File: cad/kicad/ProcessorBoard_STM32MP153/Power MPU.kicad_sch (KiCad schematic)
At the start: 1 part, among them IC301 STPMIC1BPQR

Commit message: some more caps and power specs
maybe puppy and rainbows if dont use the sw controlled PMIC. ddr dosent seem to care too much about sequencing, and the mpu sequence is 2 steps... but size :( :( :( . wheres muh leaded puckagies :(
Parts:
- added C301, C303, C305, C307: 10u, Capacitor_SMD:C_0603_1608Metric_Pad1.08x0.95mm_HandSolder, symbol Device:C_Small
- added C302, C304, C306, C308: 22u, Capacitor_SMD:C_0603_1608Metric_Pad1.08x0.95mm_HandSolder, symbol Device:C_Small
- added C309, C310, C311, C312, C313, C314: 1u, Capacitor_SMD:C_0603_1608Metric_Pad1.08x0.95mm_HandSolder, symbol Device:C_Small
- added L301, L302, L303, L304: 1u, Inductor_SMD:L_1008_2520Metric_Pad1.43x2.20mm_HandSolder, symbol Device:L_Small
- added NT301, NT302, NT303, NT304: NetTie_2, NetTie:NetTie-2_SMD_Pad0.5mm, symbol Device:NetTie_2
- added R301, R302: 3090, Resistor_SMD:R_0603_1608Metric_Pad0.98x0.95mm_HandSolder, symbol Device:R_Small_US
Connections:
- net LDO2in is gone; now on net 3v3: IC301.19 (LDO25IN)
- net SWin is gone; now on net BoostOut: IC301.37 (SWIN)
- net GND: now also C301.2, C302.2, C303.2, C304.2, C305.2, C306.2, C307.2, C308.2, C309.2, C310.2, C311.1, C312.2, C313.2, C314.1
- net LDO2out: now also C314.2
- net LDO5out: now also C313.1
- net LDO6out: now also C311.2
- net SCL: now also R301.2
- net SDA: now also R302.1
- net VLX1: now also L301.2
- net VLX2: now also L302.2
- net Vin_prim: now also C301.1, C303.1, C305.1, C307.1
- net Vout3FB: now also NT303.1
- net Vout4FB: now also NT304.1
- net LDO1and6in renamed 3v3
- net 3v3: now also C302.1, C309.1, C312.1, L304.1, NT304.2
- net LSO1out renamed LDO1out
- net LDO1out: now also C310.1
- net VLXBuck3 renamed VLX3
- net VLX3: now also L303.2
- net VLXBuck4 renamed VLX4
- net VLX4: now also L304.2
- net Vio renamed VddIO
- net VddIO: now also R301.1, R302.2
- net Vout1 renamed Vout1FB
- net Vout1FB: now also NT301.1
- net Vout2 renamed Vout2FB
- net Vout2FB: now also NT302.1
- new net V_{dd_DDR}: C306.1, L302.1, NT302.2
- new net V_{dd_IO}: C304.1, L303.1, NT303.2
- new net V_{dd_core}: C308.1, L301.1, NT301.2
- no-connect marks 0 -> 2
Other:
- note added: "unused. programmable out: [0v9,3v3], %2, 100mV steps"
- note added: "unused. programmable out: [1v8,3v3], %2, 100mV steps"

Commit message: pmic maybe
caybe bees in the halls of 3d objects. post gimp utility. hp bug kit
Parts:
- added C315, C319, C320: 10u, Capacitor_SMD:C_0603_1608Metric_Pad1.08x0.95mm_HandSolder, symbol Device:C_Small
- added C316, C317, C318, C321: 1u, Capacitor_SMD:C_0603_1608Metric_Pad1.08x0.95mm_HandSolder, symbol Device:C_Small
- added J301: Conn_01x01_Pin, Connector_PinHeader_2.54mm:PinHeader_1x01_P2.54mm_Vertical, symbol Connector:Conn_01x01_Pin
- added L305: 1u, Inductor_SMD:L_1008_2520Metric_Pad1.43x2.20mm_HandSolder, symbol Device:L_Small
- C311, C314: now not fitted; now left out of the parts list
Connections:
- net VddIO is gone; now on net V_{dd_IO}: IC301.42 (VIO), R301.1, R302.2
- net GND: now also C315.2, C316.2, C317.2, C318.2, C319.2, C320.2, C321.2
- net LDO3in: now also C308.1, L301.1, NT303.2, C319.1
- net LDO3out: now also C320.1
- net LDO4out: now also C318.1
- net PonkeyN: now also J301.1 (Pin_1)
- net VBusOTG: now also C316.1
- net VLXBoost: now also L305.1
- net V_{dd_IO}: now also NT301.2; no longer NT303.2
- net Vin_prim: now also C315.1, C317.1, L305.2
- net Vout1FB: now also NT303.1; no longer NT301.1
- net Vout3FB: now also NT301.1; no longer NT303.1
- net BoostOut: no longer names the net of IC301.34 (BOUT)
- net BoostOut: no longer IC301.37 (SWIN)
- net SWout: no longer names the net of IC301.38 (SWOUT)
- net V_{dd_DDR} renamed V_{dd_DDRQ}
- removed net V_{dd_core}: C308.1, L301.1, NT301.2
- net VrefDDR renamed V_{DDR_ref}
- net V_{DDR_ref}: now also C321.1
- no-connect marks 2 -> 5
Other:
- note added: "what to do with unused pins"
- moved on the sheet: C301, C302, C303, C304, C305, C306, C307, C308, C309, C310, C312, C313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

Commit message: respeced caps
everything out of stok :(
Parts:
- added C322, C323: 4.7u, Capacitor_SMD:C_01005_0402Metric_Pad0.57x0.30mm_HandSolder, symbol Device:C_Small
- added C324: 1u, Capacitor_SMD:C_01005_0402Metric_Pad0.57x0.30mm_HandSolder, symbol Device:C_Small
- C309, C312, C316, C317, C321: footprint Capacitor_SMD:C_0603_1608Metric_Pad1.08x0.95mm_HandSolder -> Capacitor_SMD:C_01005_0402Metric_Pad0.57x0.30mm_HandSolder; character https://ds.yuden.co.jp/TYCOMPAS/ap/detail?pn=MSASE168SB7105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 -> https://ds.murata.com/simsurfing/mlcc.html?partnumbers=%5B%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; mouser https://www.mouser.com/en/ProductDetail/Samsung-Electro-Mec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 -> https://www.mouser.com/en/ProductDetail/Murata-Electronics/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; unit x1 0.29 -> 0.11; unit x10 0.168 -> 0.04
- C310, C311, C313, C314, C318: value 1u -> 4.7u; footprint Capacitor_SMD:C_0603_1608Metric_Pad1.08x0.95mm_HandSolder -> Capacitor_SMD:C_01005_0402Metric_Pad0.57x0.30mm_HandSolder; character https://ds.yuden.co.jp/TYCOMPAS/ap/detail?pn=MSASE168SB7105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 -> https://ds.murata.com/simsurfing/mlcc.html?partnumbers=%5B%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; mouser https://www.mouser.com/en/ProductDetail/Samsung-Electro-Mec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 -> https://www.mouser.com/en/ProductDetail/Murata-Electronics/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; unit x1 0.29 -> 0.047; unit x10 0.168 -> 0.11
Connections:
- net AGnd is gone; now on net GND: IC301.41 (AGND)
- net GND: now also C311.2, C314.2, C322.2, C323.2, C324.2; no longer C311.1, C314.1
- net InternalLDO: now also C323.1
- net LDO2out: now also C314.1; no longer C314.2
- net LDO6out: now also C311.1; no longer C311.2
- net VBusOTG: now also C324.1
- net Vin_prim: now also C322.1
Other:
- moved on the sheet: IC301, J301, R301, R302

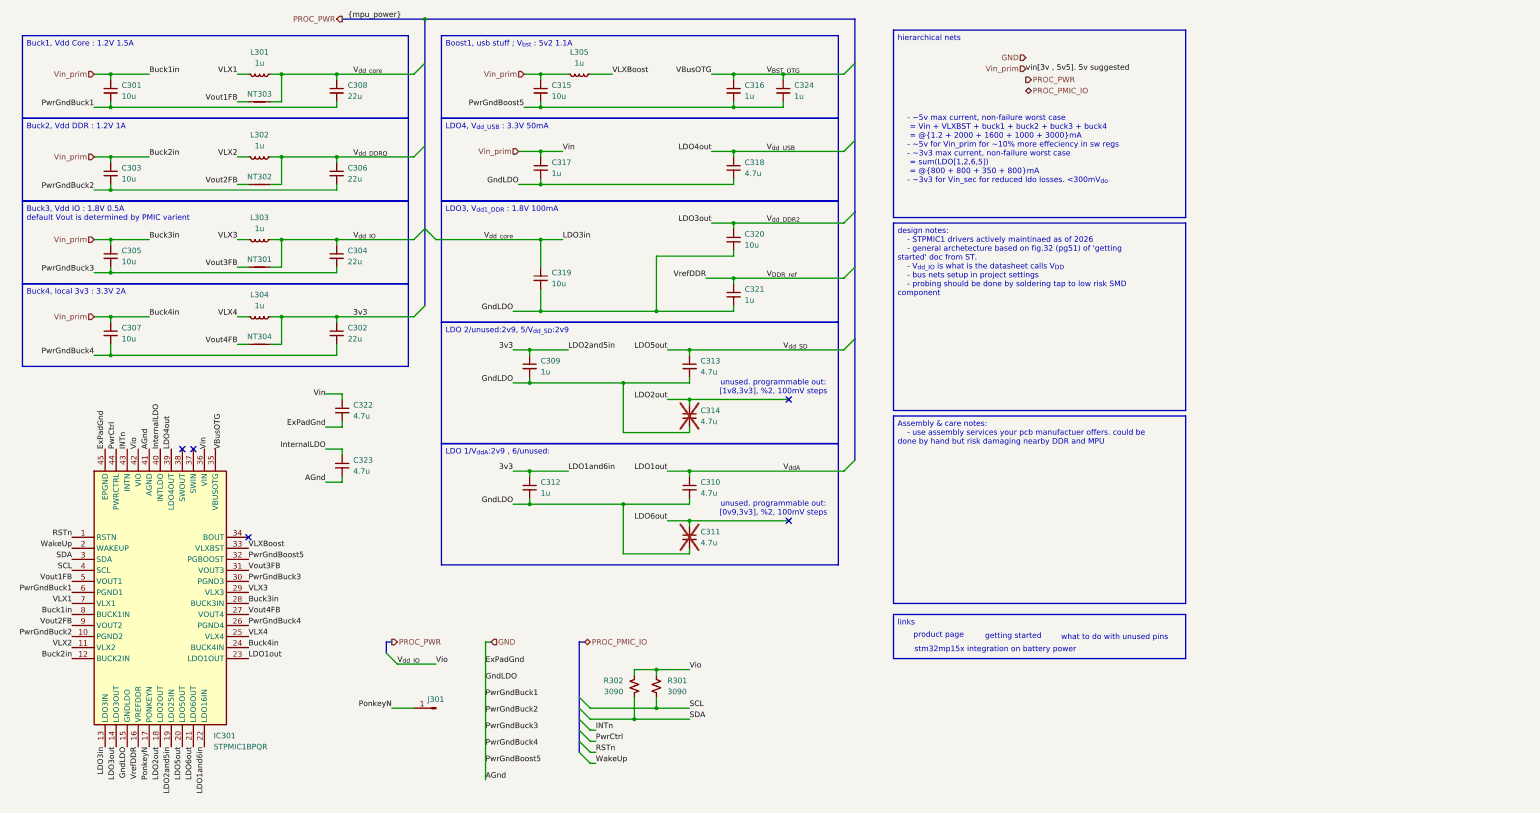
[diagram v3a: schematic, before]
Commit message: verified jlc price category
~[32, 50]usd for 5 boards. includes impedence control. though must be 1oz top & bottom layers, 0.5oz inner layers . goes up at least $10usd for different pours
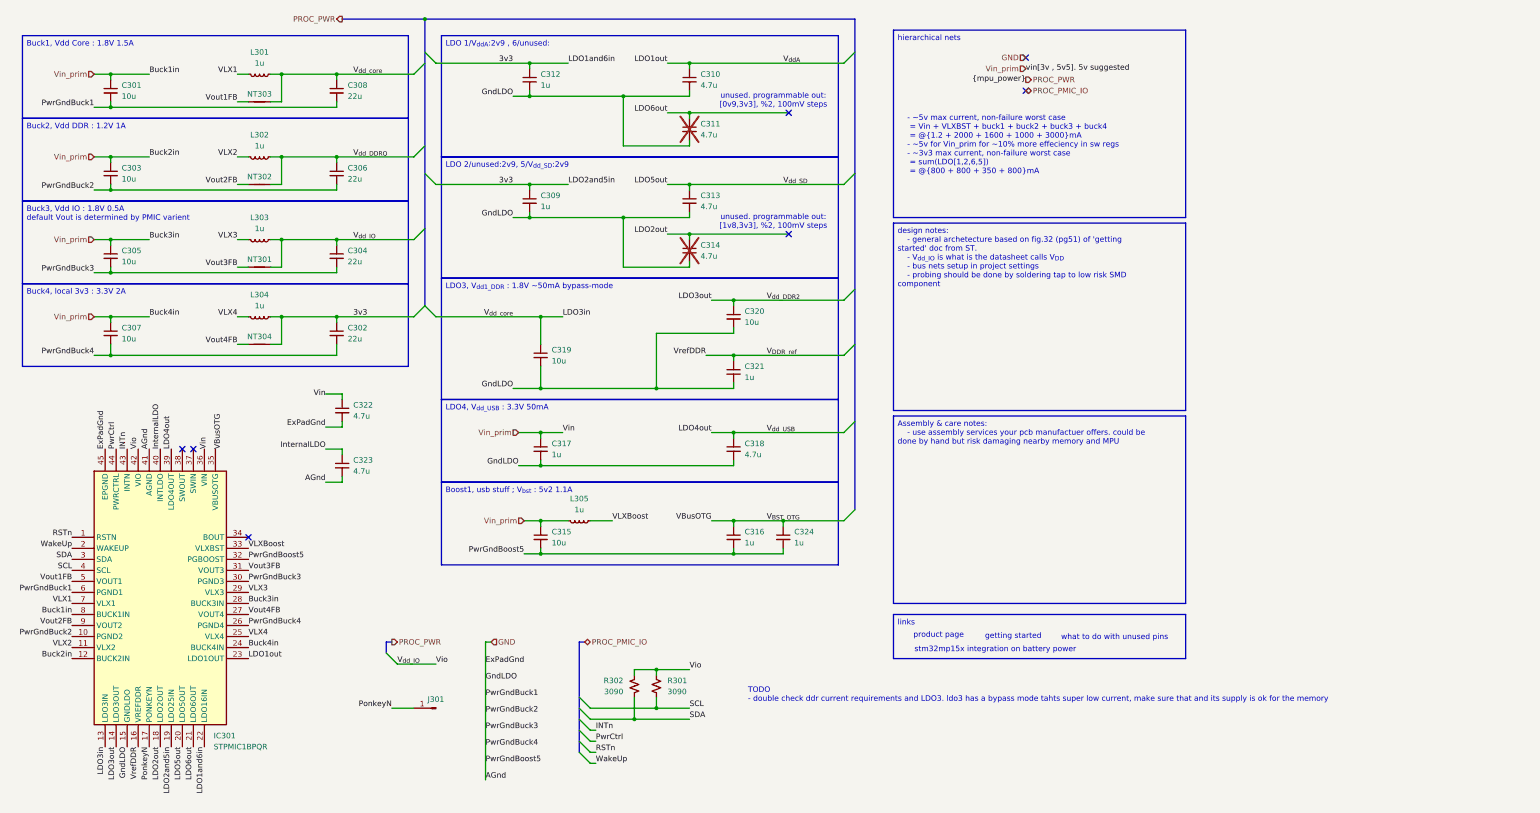
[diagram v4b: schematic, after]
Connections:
- no-connect marks 5 -> 7
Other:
- note added: "TODO - double check ddr current requirements and LDO3. ldo3 has a bypass mode tahts super low current, make sure that and its supply is ok for the memory"
- moved on the sheet: C309, C310, C311, C312, C313, C314, C315, C316, C317, C318, C319, C320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

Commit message: mpu power connections
about mpu, apparently onboard usb supply has a requirement for the onboard ldo's to be happy, so u have to tap out 2 deticated pins. and theres also a power off sequence as well???
1v8 life looking better every day, 3v3(>2v9) trenches over there
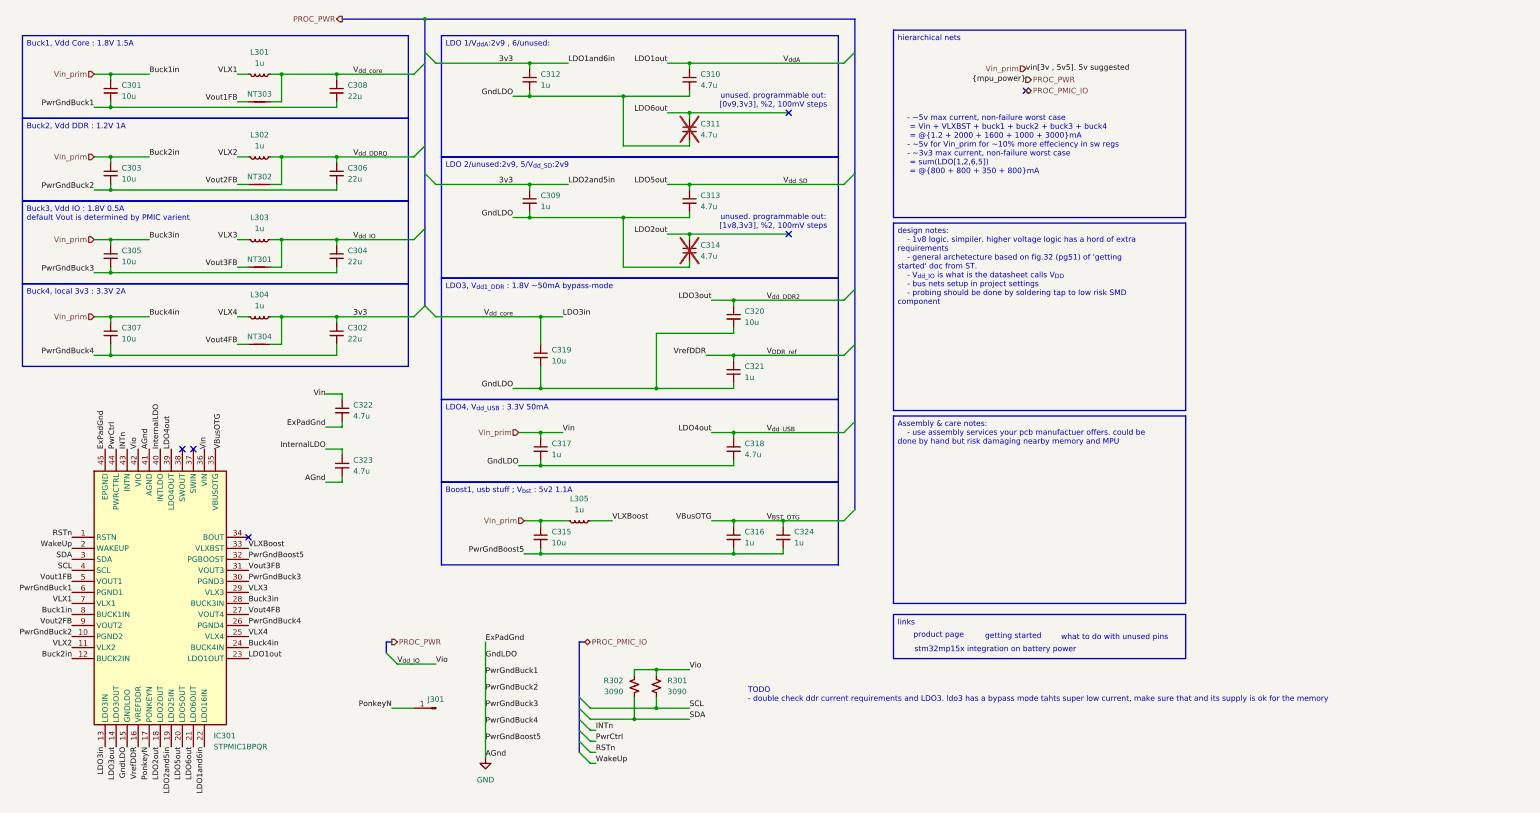
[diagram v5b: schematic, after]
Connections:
- no-connect marks 7 -> 6
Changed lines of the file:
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@@
 		)
 	)
-	(text_box "design notes:\n	- general archetecture based on fig.32 (pg51) of 'getting started' doc from ST.\n	- V_{dd_IO} is what is the datasheet calls V_{DD}\n	- bus nets setup in project settings\n	- probing should be done by soldering tap to low risk SMD component"
+	(text_box "design notes:\n	- 1v8 logic. simpiler. higher voltage logic has a hord of extra requirements\n	- general archetecture based on fig.32 (pg51) of 'getting started' doc from ST.\n	- V_{dd_IO} is what is the datasheet calls V_{DD}\n	- bus nets setup in project settings\n	- probing should be done by soldering tap to low risk SMD component"
 		(exclude_from_sim no)
 		(at 215.9 63.5 0)
@@
 	)
 	(no_connect
-		(at 246.38 25.4)
-	)
-	(no_connect
 		(at 191.77 38.1)
 	)
@@
 		)
 	)
+	(wire
+		(pts
+			(xy 121.92 160.02) (xy 121.92 186.69)
+		)
+		(stroke
+			(width 0)
+			(type default)
+		)
+	)
 	(bus
 		(pts
@@
 	(wire
 		(pts
-			(xy 123.19 160.02) (xy 121.92 160.02)
-		)
-		(stroke
-			(width 0)
-			(type default)
-		)
-	)
-	(wire
-		(pts
 			(xy 134.62 139.7) (xy 134.62 138.43)
 		)
@@
 	(wire
 		(pts
-			(xy 121.92 160.02) (xy 121.92 191.77)
-		)
-		(stroke
-			(width 0)
-			(type default)
-		)
-	)
-	(wire
-		(pts
 			(xy 74.93 48.26) (xy 74.93 54.61)
 		)
@@
 	)
 	(label "PwrGndBuck4"
-		(at 121.92 184.15 0)
+		(at 121.92 179.07 0)
 		(effects
 			(font
@@
 	)
 	(label "PwrGndBoost5"
-		(at 121.92 187.96 0)
+		(at 121.92 182.88 0)
 		(effects
 			(font
@@
 	)
 	(label "PwrGndBuck3"
-		(at 121.92 180.34 0)
+		(at 121.92 175.26 0)
 		(effects
 			(font
@@
 	)
 	(label "GndLDO"
-		(at 121.92 168.91 0)
+		(at 121.92 163.83 0)
 		(effects
 			(font
@@
 	)
 	(label "PwrGndBuck2"
-		(at 121.92 176.53 0)
+		(at 121.92 171.45 0)
 		(effects
 			(font
@@
 	)
 	(label "PwrGndBuck1"
-		(at 121.92 172.72 0)
+		(at 121.92 167.64 0)
 		(effects
 			(font
@@
 	)
 	(label "AGnd"
-		(at 121.92 191.77 0)
+		(at 121.92 186.69 0)
 		(effects
 			(font
@@
 	)
 	(label "ExPadGnd"
-		(at 121.92 165.1 0)
+		(at 121.92 160.02 0)
 		(effects
 			(font
@@
 		)
 	)
-	(hierarchical_label "GND"
-		(shape input)
-		(at 246.38 25.4 180)
-		(effects
-			(font
-				(size 1.27 1.27)
-			)
-			(justify right)
-		)
-	)
 	(hierarchical_label "Vin_prim"
 		(shape input)
@@
 		)
 	)
-	(hierarchical_label "GND"
-		(shape input)
-		(at 123.19 160.02 0)
-		(effects
-			(font
-				(size 1.27 1.27)
-			)
-			(justify left)
-		)
-	)
 	(symbol
 		(lib_id "Device:NetTie_2")
@@
 					(unit 1)
 				)
+			)
+		)
+	)
+	(symbol
+		(lib_id "power:GND")
+		(at 121.92 186.69 0)
+		(unit 1)
+		(body_style 1)
+		(exclude_from_sim no)
+		(in_bom yes)
+		(on_board yes)
+		(in_pos_files yes)
+		(dnp no)
+		(fields_autoplaced yes)
+		(property "Reference" "#PWR0301"
+			(at 121.92 193.04 0)
+			(hide yes)
+			(show_name no)
+			(do_not_autoplace no)
+			(effects
+				(font
+					(size 1.27 1.27)
+				)
+			)
+		)
+		(property "Value" "GND"
+			(at 121.92 191.77 0)
+			(show_name no)
+			(do_not_autoplace no)
+			(effects
+				(font
+					(size 1.27 1.27)
+				)
+			)
+		)
+		(property "Footprint" ""
+			(at 121.92 186.69 0)
+			(hide yes)
+			(show_name no)
+			(do_not_autoplace no)
+			(effects
+				(font
+					(size 1.27 1.27)
+				)
+			)
+		)
+		(property "Datasheet" ""
+			(at 121.92 186.69 0)
+			(hide yes)
+			(show_name no)
+			(do_not_autoplace no)
+			(effects
+				(font
+					(size 1.27 1.27)
+				)
+			)
+		)
+		(property "Description" "Power symbol creates a global label with name \"GND\" , ground"
+			(at 121.92 186.69 0)
+			(hide yes)
+			(show_name no)
+			(do_not_autoplace no)
+			(effects
+				(font
+					(size 1.27 1.27)
+				)
+			)
+		)
+		(pin "1"
+		)
+		(instances
+			(project "ProcessorBoard_STM32MP153"
+				(path "/e63e39d7-6ac0-4ffd-8aa3-1841a4541b55/06ad9cc8-e1a1-474d-84d3-806ac75aa67c"
+					(reference "#PWR0301")
+					(unit 1)
+				)

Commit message: mr przudent get down
a thrid DDR voltage requirement has hit the power plane.
the cost of 11$ ram is apparently 3 distinct power nets :( .
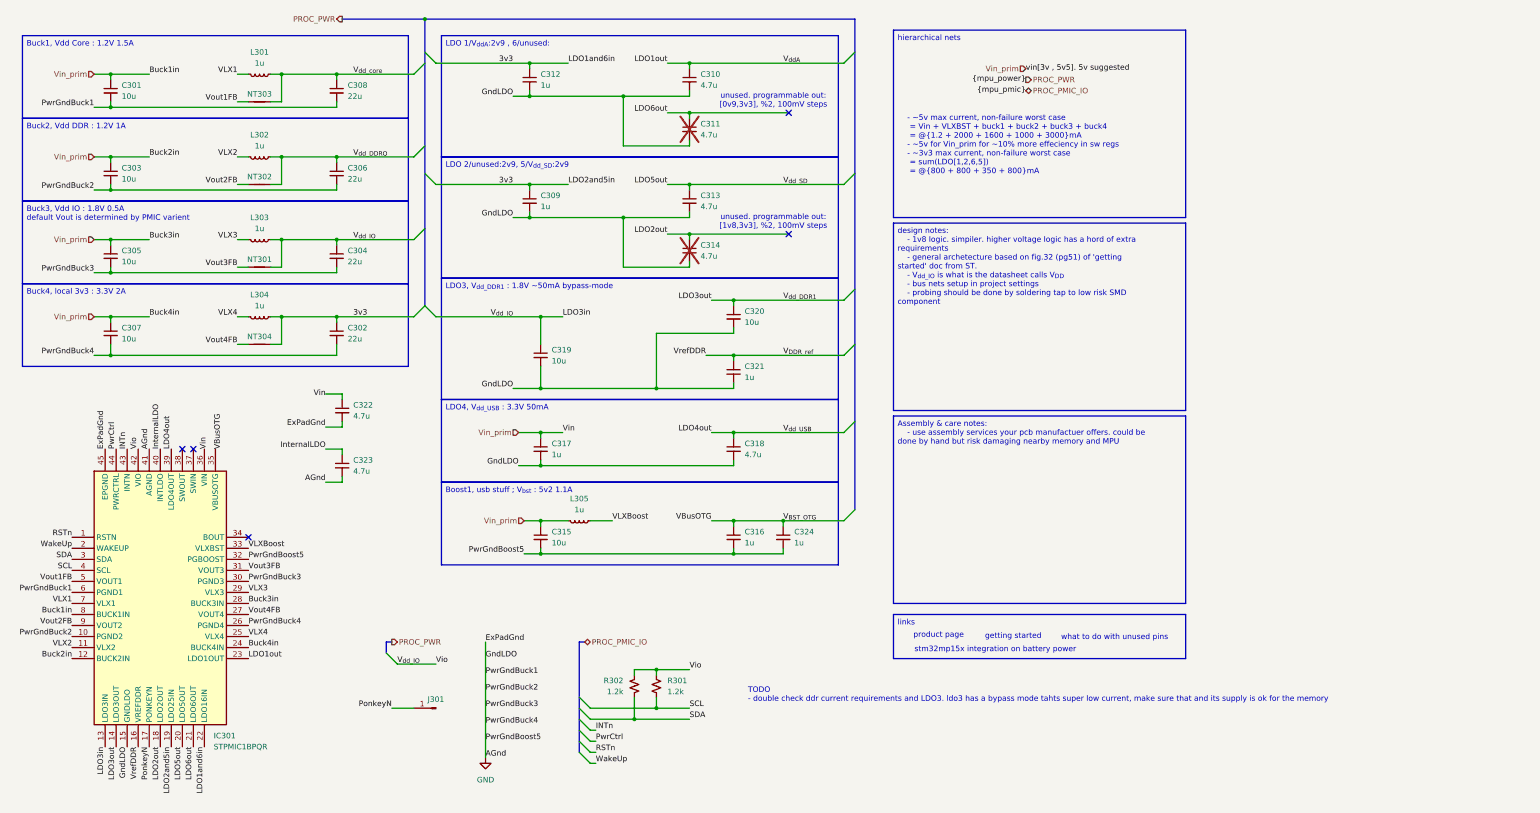
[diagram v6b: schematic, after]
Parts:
- R301, R302: value 3090 -> 1.2k; mouser https://www.mouser.com/en/ProductDetail/Walsin/WR06X392-JTL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 -> https://www.mouser.com/en/ProductDetail/TE-Connectivity-Hol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; unit x1 0.1 -> 0.10; unit x10 0.08 -> 0.018; unit x100 0.60 -> 0.017
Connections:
- net V_{dd_IO} is gone; now on net LDO3in: C304.1, IC301.42 (VIO), L303.1, NT301.2, R301.1, R302.2
- net LDO3in: no longer C308.1, L301.1, NT303.2
- new net V_{dd_core}: C308.1, L301.1, NT303.2
- no-connect marks 6 -> 5
